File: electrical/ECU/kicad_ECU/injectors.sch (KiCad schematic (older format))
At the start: 11 parts

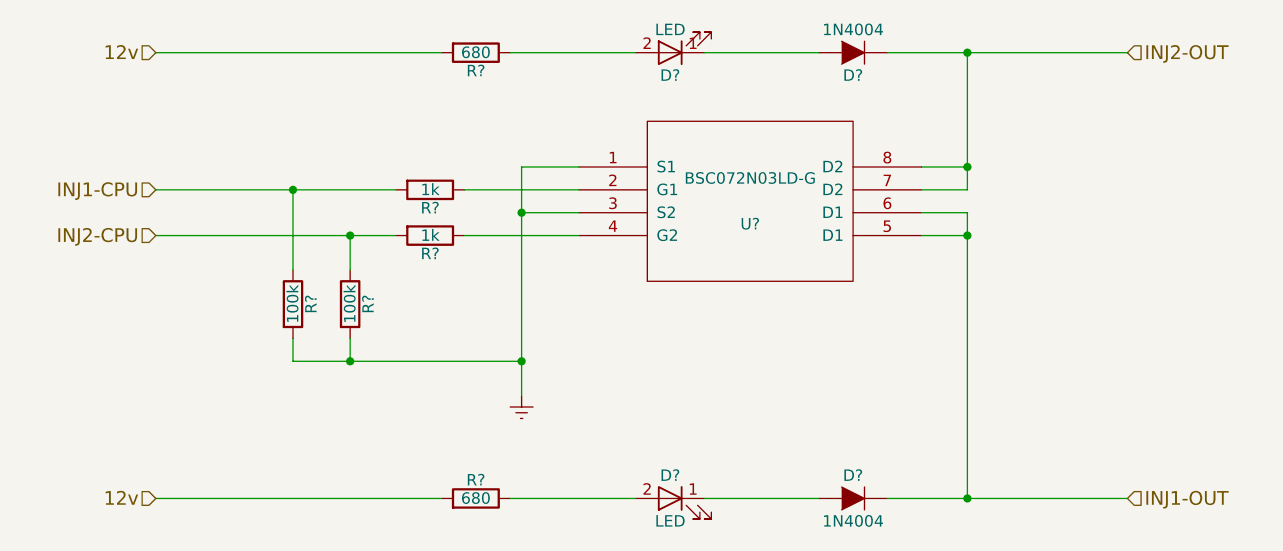
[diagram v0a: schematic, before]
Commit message: fixed some naming errors and initial round of double checking
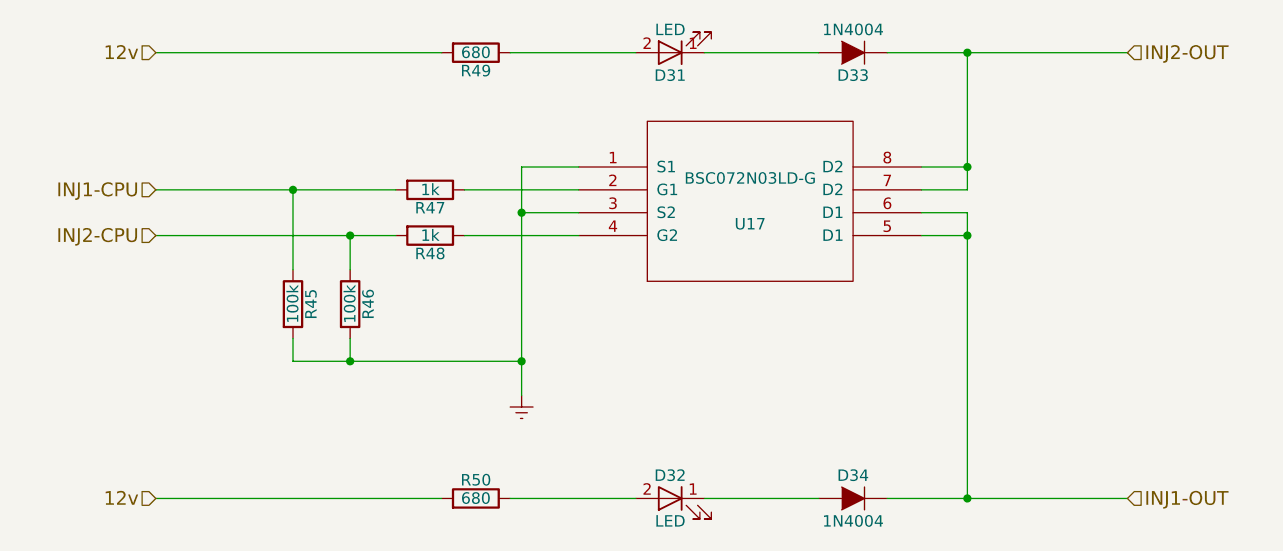
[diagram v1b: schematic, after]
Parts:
- gave numbers to parts that had none: 11
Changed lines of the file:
@@
 $Descr A4 11693 8268
 encoding utf-8
-Sheet 18 33
+Sheet 22 33
 Title "Injectors"
 Date ""
@@
 $EndDescr
 $Comp
-L BSC072N03LD-G U?
+L BSC072N03LD-G U17
 U 1 1 5977A542
 P 7250 3250
-F 0 "U?" H 7250 3150 50  0000 C CNN
+F 0 "U17" H 7250 3150 50  0000 C CNN
 F 1 "BSC072N03LD-G" H 7250 3350 50  0000 C CNN
 F 2 "MODULE" H 7250 3250 50  0001 C CNN
@@
 $EndComp
 $Comp
-L Earth #PWR?
+L Earth #PWR51
 U 1 1 5977A637
 P 6250 4100
-F 0 "#PWR?" H 6250 3850 50  0001 C CNN
+F 0 "#PWR51" H 6250 3850 50  0001 C CNN
 F 1 "Earth" H 6250 3950 50  0001 C CNN
 F 2 "" H 6250 4100 50  0001 C CNN
@@
 $EndComp
 $Comp
-L R R?
+L R R47
 U 1 1 5977A67E
 P 5850 3200
-F 0 "R?" V 5930 3200 50  0000 C CNN
+F 0 "R47" V 5930 3200 50  0000 C CNN
 F 1 "1k" V 5850 3200 50  0000 C CNN
 F 2 "" V 5780 3200 50  0001 C CNN
@@
 $EndComp
 $Comp
-L R R?
+L R R48
 U 1 1 5977A6ED
 P 5850 3400
-F 0 "R?" V 5930 3400 50  0000 C CNN
+F 0 "R48" V 5930 3400 50  0000 C CNN
 F 1 "1k" V 5850 3400 50  0000 C CNN
 F 2 "" V 5780 3400 50  0001 C CNN
@@
 $EndComp
 $Comp
-L R R?
+L R R46
 U 1 1 5977A71B
 P 5500 3700
-F 0 "R?" V 5580 3700 50  0000 C CNN
+F 0 "R46" V 5580 3700 50  0000 C CNN
 F 1 "100k" V 5500 3700 50  0000 C CNN
 F 2 "" V 5430 3700 50  0001 C CNN
@@
 $EndComp
 $Comp
-L R R?
+L R R45
 U 1 1 5977A73E
 P 5250 3700
-F 0 "R?" V 5330 3700 50  0000 C CNN
+F 0 "R45" V 5330 3700 50  0000 C CNN
 F 1 "100k" V 5250 3700 50  0000 C CNN
 F 2 "" V 5180 3700 50  0001 C CNN
@@
 INJ2-CPU
 $Comp
-L D D?
+L D D33
 U 1 1 5977A82B
 P 7700 2600
-F 0 "D?" H 7700 2700 50  0000 C CNN
+F 0 "D33" H 7700 2700 50  0000 C CNN
 F 1 "1N4004" H 7700 2500 50  0000 C CNN
 F 2 "" H 7700 2600 50  0001 C CNN
@@
 $EndComp
 $Comp
-L LED-RESCUE-airhead_ecu D?
+L LED-RESCUE-airhead_ecu D31
 U 1 1 5977A89D
 P 6900 2600
-F 0 "D?" H 6900 2700 50  0000 C CNN
+F 0 "D31" H 6900 2700 50  0000 C CNN
 F 1 "LED" H 6900 2500 50  0000 C CNN
 F 2 "" H 6900 2600 50  0001 C CNN
@@
 $EndComp
 $Comp
-L R R?
+L R R49
 U 1 1 5977A8EA
 P 6050 2600
-F 0 "R?" V 6130 2600 50  0000 C CNN
+F 0 "R49" V 6130 2600 50  0000 C CNN
 F 1 "680" V 6050 2600 50  0000 C CNN
 F 2 "" V 5980 2600 50  0001 C CNN
@@
 12v
 $Comp
-L D D?
+L D D34
 U 1 1 5977AA87
 P 7700 4550
-F 0 "D?" H 7700 4650 50  0000 C CNN
+F 0 "D34" H 7700 4650 50  0000 C CNN
 F 1 "1N4004" H 7700 4450 50  0000 C CNN
 F 2 "" H 7700 4550 50  0001 C CNN
@@
 $EndComp
 $Comp
-L LED-RESCUE-airhead_ecu D?
+L LED-RESCUE-airhead_ecu D32
 U 1 1 5977AA8D
 P 6900 4550
-F 0 "D?" H 6900 4650 50  0000 C CNN
+F 0 "D32" H 6900 4650 50  0000 C CNN
 F 1 "LED" H 6900 4450 50  0000 C CNN
 F 2 "" H 6900 4550 50  0001 C CNN
@@
 $EndComp
 $Comp
-L R R?
+L R R50
 U 1 1 5977AA93
 P 6050 4550
-F 0 "R?" V 6130 4550 50  0000 C CNN
+F 0 "R50" V 6130 4550 50  0000 C CNN
 F 1 "680" V 6050 4550 50  0000 C CNN
 F 2 "" V 5980 4550 50  0001 C CNN
